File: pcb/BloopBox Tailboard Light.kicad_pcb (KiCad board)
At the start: 4 copper layers, 60 x 49 mm, 64 parts, among them J1 USB_C_Receptacle_Power, J2 Barrel_Jack, J3 Mainboard, Q1 AO3401A, Q3 AO3401A, Q5 AO3401A, SW1 Button1, SW2 Button2, U1 HT7533-1, U4 TPS54302, U5 LM393APWR, U6 LM393APWR

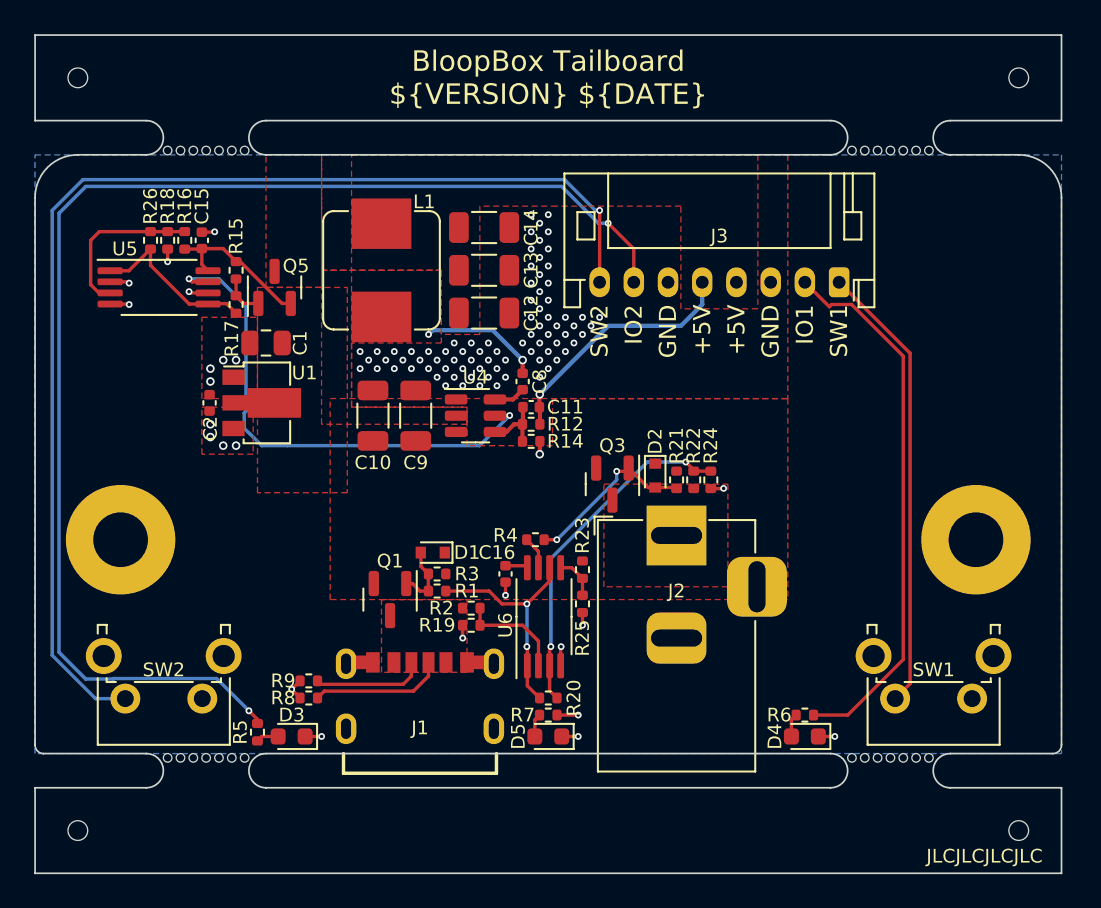
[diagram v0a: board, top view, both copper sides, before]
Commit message: feat: remove active circuitry from PCB
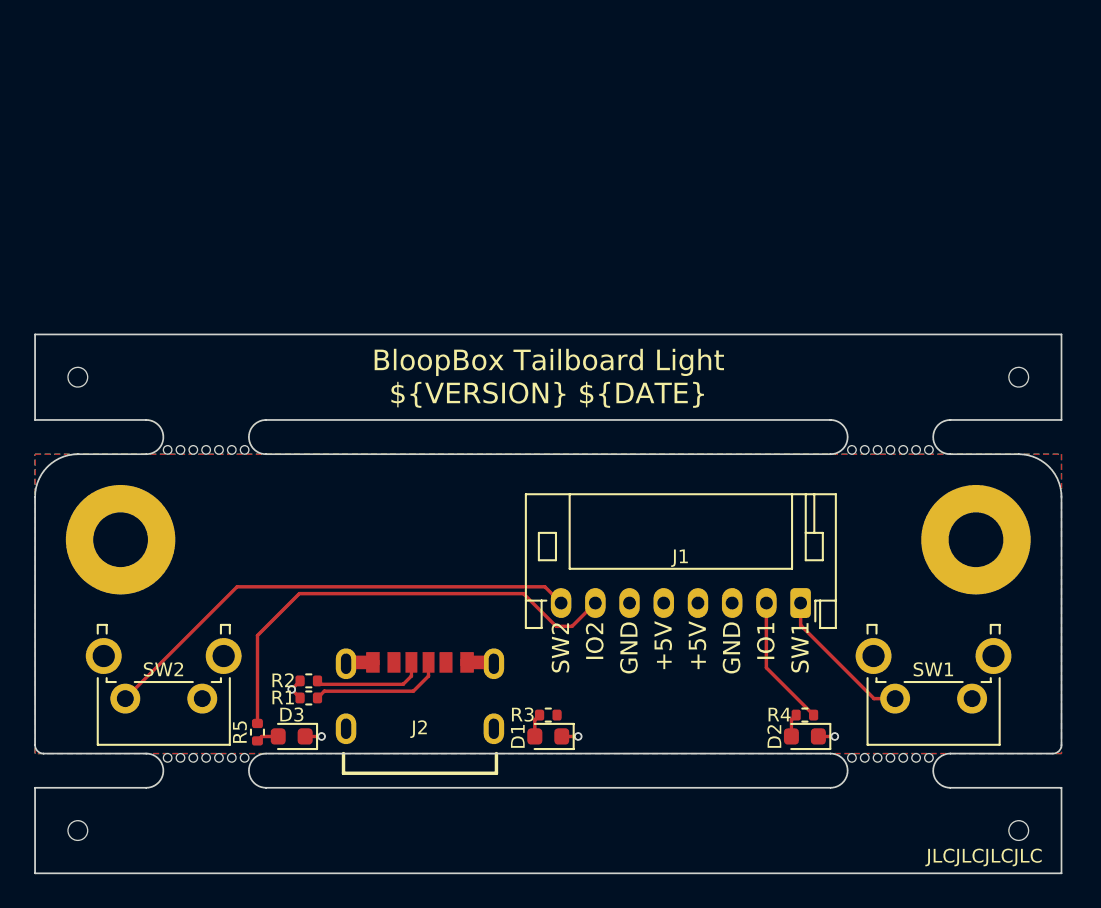
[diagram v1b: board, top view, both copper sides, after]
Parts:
- removed C1: 10uF, Capacitor_SMD:C_0805_2012Metric
- removed C10, C9: 10uF, Capacitor_SMD:C_1206_3216Metric
- removed C11: 100pF, Capacitor_SMD:C_0402_1005Metric
- removed C12, C13, C14: 22uF, Capacitor_SMD:C_1206_3216Metric
- removed C15, C16, C8: 100nF, Capacitor_SMD:C_0402_1005Metric
- removed C2: 10uF, Capacitor_SMD:C_0402_1005Metric
- removed the D1 at (138.2, 78.2)
- removed the D2 at (151.2, 73.8)
- removed the J2 at (152.5, 77.2)
- removed L1: 6.8uH, Inductor_SMD:L_Bourns_SRP7028A_7.3x6.6mm
- removed Q1, Q3, Q5: AO3401A, Package_TO_SOT_SMD:SOT-23
- removed the R1 at (138.5, 80.5)
- removed R12: 150k, Resistor_SMD:R_0402_1005Metric
- removed R14, R16: 20k, Resistor_SMD:R_0402_1005Metric
- removed R15, R19, R22, R23, R24, R25: 47k, Resistor_SMD:R_0402_1005Metric
- removed R17: 10k, Resistor_SMD:R_0402_1005Metric
- removed R18, R21: 33k, Resistor_SMD:R_0402_1005Metric
- removed the R2 at (140.5, 81.5)
- removed R20, R26: 1M, Resistor_SMD:R_0402_1005Metric
- removed the R3 at (138.5, 79.5)
- removed the R4 at (144.2, 77.5)
- removed U1: HT7533-1, Package_TO_SOT_SMD:SOT-89-3
- removed U4: TPS54302, Package_TO_SOT_SMD:SOT-23-6
- removed U5, U6: LM393APWR, Package_SO:TSSOP-8_4.4x3mm_P0.65mm
- R3: renamed from R7; value 680R -> 1k5
- moved G*** 22.6 mm to (138.8, 77.5)
- moved J1 18.9 mm to (159.8, 81.2)
- moved REF** 17.5 mm to (172.5, 68.0)
- moved REF** 17.5 mm to (117.5, 68.0)
- moved mouse-bite-2mm-slot 17.5 mm to (165.0, 71.5)
- moved mouse-bite-2mm-slot 17.5 mm to (125.0, 71.5)
- moved REF** 8.00 mm to (130.0, 78.5)
- renumbered D5 to D1, D4 to D2, J3 to J1, J1 to J2, R8 to R1, R9 to R2, R6 to R4
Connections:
- J2 pad A9: /USB-IN -> +5V
- J2 pad B9: /USB-IN -> +5V
- R3 pad 1: +3V3 -> +5V
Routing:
- net /IO2: track 76.9 -> 27.3 mm, vias 2 -> 0
- net /Button2: track 69.0 -> 28.6 mm, vias 1 -> 0
- net /Buck Regulator/TPSen: track 29.9 -> 0.00 mm, vias 2 -> 0
- net /IO1: track 32.0 -> 7.69 mm
- net /Power Input Selector/DCsense: track 20.3 -> 0.00 mm, vias 2 -> 0
- net /Button1: track 26.4 -> 8.60 mm
- net +5V: track 14.7 -> 0.00 mm, vias 1 -> 0
- net /Power Input Selector/USBctrl: track 13.5 -> 0.00 mm, vias 2 -> 0
- net VBUS: track 10.3 -> 0.00 mm
- net /Power Input Selector/DCg: track 10.3 -> 0.00 mm, vias 2 -> 0
- net /Buck Regulator/BPctrl: track 9.98 -> 0.00 mm
- net /Buck Regulator/BPfb: track 9.64 -> 0.00 mm
- net GND: track 15.0 -> 7.50 mm, vias 98 -> 4
- net /Buck Regulator/SW: track 7.10 -> 0.00 mm, vias 2 -> 0
- net /Power Input Selector/USBsense: track 6.24 -> 0.00 mm
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- removed copper zone on F.Cu, net +3V3
- removed copper zone on In2.Cu, net +3V3
- removed copper zone on F.Cu, net /Buck Regulator/SW
- removed copper zone on F.Cu, net /DC-IN
- removed copper zone on F.Cu, net /USB-IN
- removed copper zone on F.Cu, net GND
- removed copper zone on In1.Cu, net GND
- removed copper zone on F.Cu, net VBUS
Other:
- board size 60 x 49 mm -> 60 x 31.5 mm
- copper layers 4 -> 2

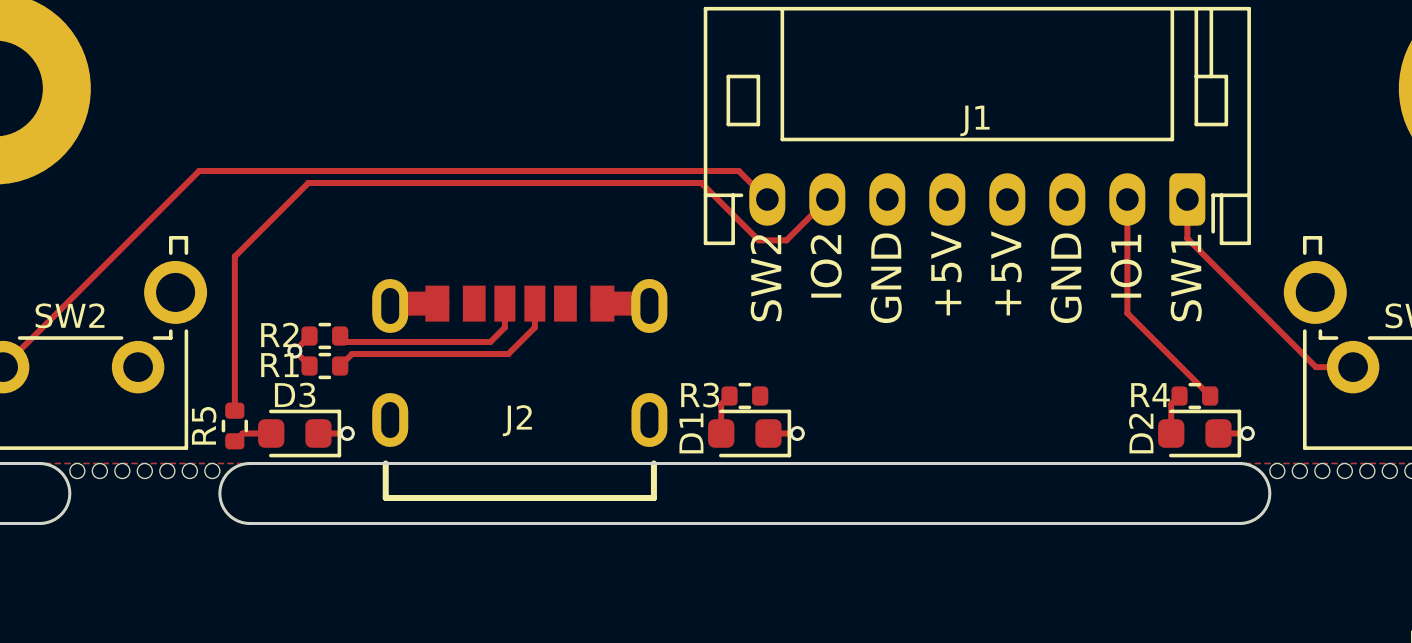
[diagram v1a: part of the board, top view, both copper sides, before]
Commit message: fix: change resistors to 0603 footptint
Changing the resistor footprints to 0603 to make hand-soldering easier, since this board does not have the size restraints of the full version of the Tailboard
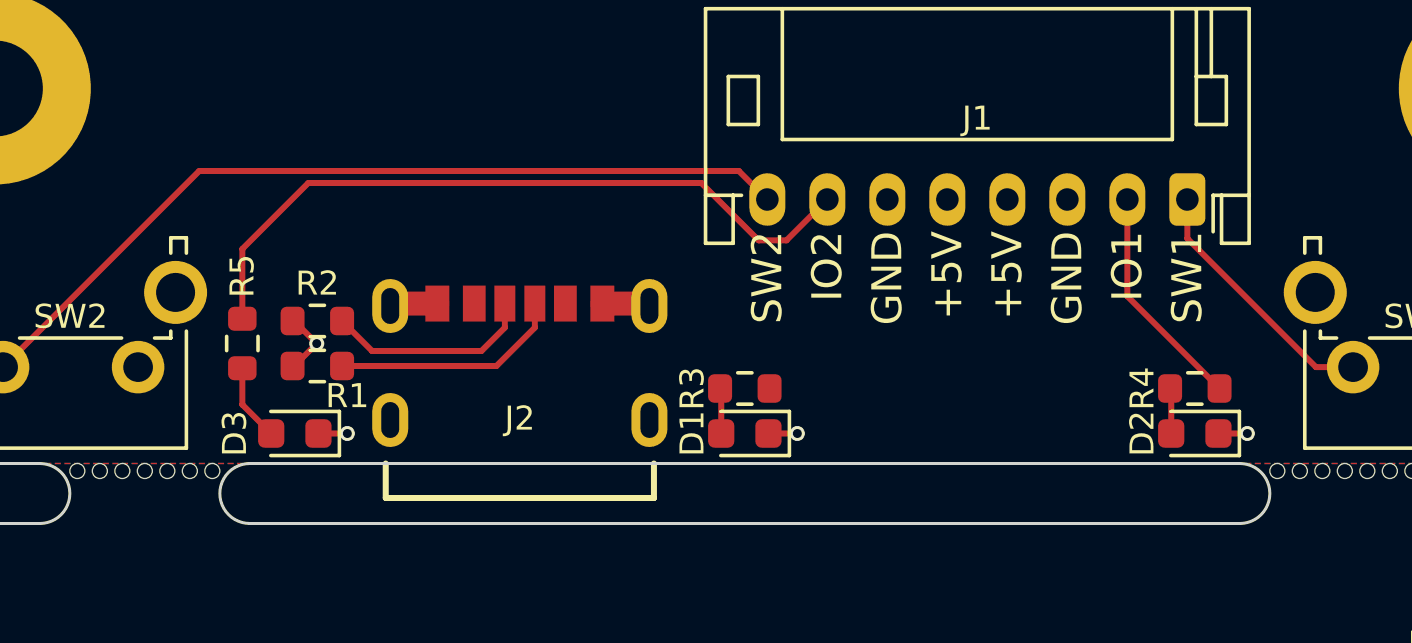
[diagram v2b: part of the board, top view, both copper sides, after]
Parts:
- R1, R2, R3, R4, R5: footprint Resistor_SMD:R_0402_1005Metric -> Resistor_SMD:R_0603_1608Metric
- moved R5 2.76 mm to (128.2, 86.0)
- moved R2 0.56 mm to (130.8, 85.2)
- moved R1 0.25 mm to (130.8, 86.8)
- moved R3 0.25 mm to (145.0, 87.5)
- moved R4 0.25 mm to (160.0, 87.5)
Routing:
- net /IO2: track 27.3 -> 24.1 mm
- net Net-(D3-Pad2): track 1.32 -> 2.57 mm
- net GND: track 7.50 -> 8.33 mm

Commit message: chore: update to KiCad 8
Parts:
- H1, H2: footprint MountingHole:MountingHole_3.2mm_M3_Pad -> MountingHole:MountingHole_3.2mm_M3
